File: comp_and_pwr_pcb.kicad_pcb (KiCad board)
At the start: 4 copper layers, 50 x 88.5 mm, 145 parts, among them IC1 TPS5430MDDAREP, IC2 ICM-42688-P, IC3 LTC4415EDHC#TRPBF, IC4 TPS259531DSGR, IC5 BMP388, IC6 W25Q32JVSSIQ, J1 USB4216-03-A, J10 Conn_01x02, J11 Conn_Coaxial, J12 Conn_Coaxial, J2 BATTERY_CONN, J3 SWD_CONN, J4 SERVO_CONN_01, J5 SERVO_CONN_02, J6 DM3AT-SF-PEJM5, J7 CAMERA_CONN_01, J8 CAMERA_CONN_02, J9 Conn_01x02, Q1 2N3904, Q2 BSS138, Q3 BSS138, Q4 BC847B, Q5 BC847B, Q6 MMBT3904, Q7 MMBT3904, SW1 SW_Push, SW2 SW_Push, U1 RP2040, U2 MAX-M10S, U3 MP2307DN-LF-Z, Y1 ABMM2-12.000MHZ-D1-T

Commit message: Changes
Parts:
- removed C14, C22: 10uF, Capacitor_SMD:C_0402_1005Metric
- removed C21, C25: 100nF, Capacitor_SMD:C_0402_1005Metric
- removed IC2: ICM-42688-P, ICM-42688-P:IIM42352
- removed JP4: SolderJumper_3_Open, Jumper:SolderJumper-3_P1.3mm_Open_Pad1.0x1.5mm
- removed Q7: MMBT3904, Package_TO_SOT_SMD:SOT-23
- added C26: 100nF, Capacitor_SMD:C_0402_1005Metric, F.Cu at (136.8, 152.5)
- added C27: 10uF, Capacitor_SMD:C_0402_1005Metric, F.Cu at (136.8, 151.0)
- added C31: 10uF, Capacitor_SMD:C_0402_1005Metric, F.Cu at (136.8, 144.5)
- added C32: 100nF, Capacitor_SMD:C_0402_1005Metric, F.Cu at (136.8, 145.8)
- added JP2: SolderJumper_3_Open, Jumper:SolderJumper-3_P1.3mm_Open_Pad1.0x1.5mm, F.Cu at (135.3, 141.5)
- added Q8: DMP3013SFV, Package_SON:Diodes_PowerDI3333-8, F.Cu at (116.5, 131.5)
- added U4: LSM6DSO, LSM6DSO:LGA14L, F.Cu at (135.8, 148.5)
- Q6: value MMBT3904 -> DMP3013SFV; footprint Package_TO_SOT_SMD:SOT-23 -> Package_SON:Diodes_PowerDI3333-8
- moved D3 6.02 mm to (115.0, 96.5)
- moved Q6 4.55 mm to (116.5, 136.0)
- moved J4 0.46 mm to (140.0, 109.0)
- moved D5 0.41 mm to (133.3, 94.0), turned to 180 degrees
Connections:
- Q6 pad 1: Net-(Q6-B) -> +BATT
- Q6 pad 3: Net-(J10-Pin_1) -> +BATT
- R58 pad 1: Net-(Q6-B) -> Net-(Q8-G)
- R62 pad 1: Net-(Q7-B) -> Net-(Q6-G)
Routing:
- net Net-(Q6-G): track 0.00 -> 11.0 mm
- net GND: track 267.5 -> 258.3 mm
- net Net-(IC2-AP_SDO_/_AP_AD0): track 7.78 -> 0.00 mm
- net Net-(JP2-C): track 0.00 -> 7.17 mm, vias 0 -> 2
- net Net-(Q8-G): track 0.00 -> 5.21 mm
- net +BATT: track 178.7 -> 182.7 mm, vias 5 -> 4
- net Net-(Q7-B): track 4.86 -> 1.34 mm, vias 2 -> 1
- net Net-(Q6-B): track 2.64 -> 0.00 mm
- net Net-(D3-A2): track 30.0 -> 28.0 mm, vias 0 -> 1
- net Net-(J10-Pin_1): track 56.7 -> 57.9 mm
- net /I2C_SCL: track 98.5 -> 99.6 mm, vias 6 -> 7
- net /SWDIO: track 44.7 -> 45.5 mm, vias 4 -> 5
- net Net-(J9-Pin_1): track 24.7 -> 25.5 mm
- net /WSP_SS: track 53.0 -> 53.6 mm
- net +3.3V: track 243.7 -> 244.2 mm, vias 10 -> 12
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
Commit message: added MPN and manufacturer
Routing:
- net Net-(Q7-B): track 1.34 -> 0.00 mm, vias 1 -> 0
- net (no net): track 0.00 -> 1.34 mm, vias 0 -> 1

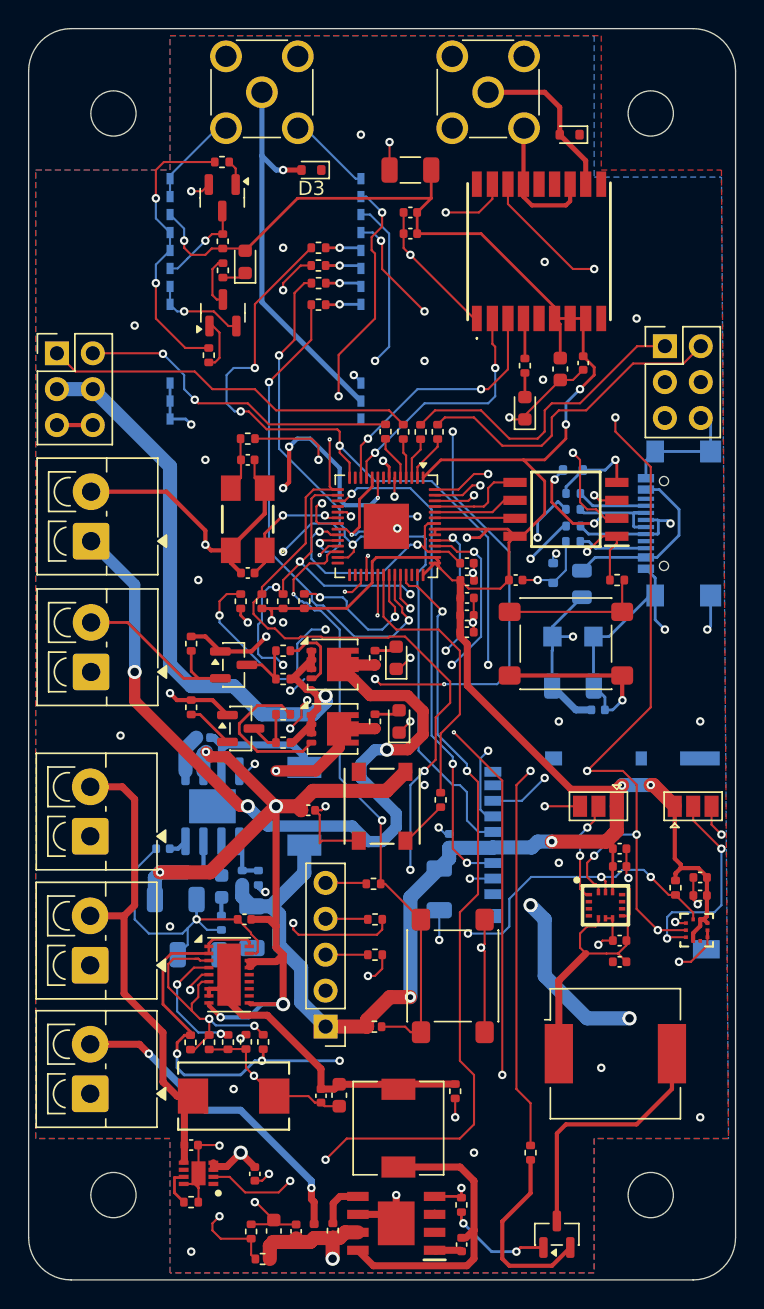
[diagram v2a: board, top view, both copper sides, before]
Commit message: Silkscreen added
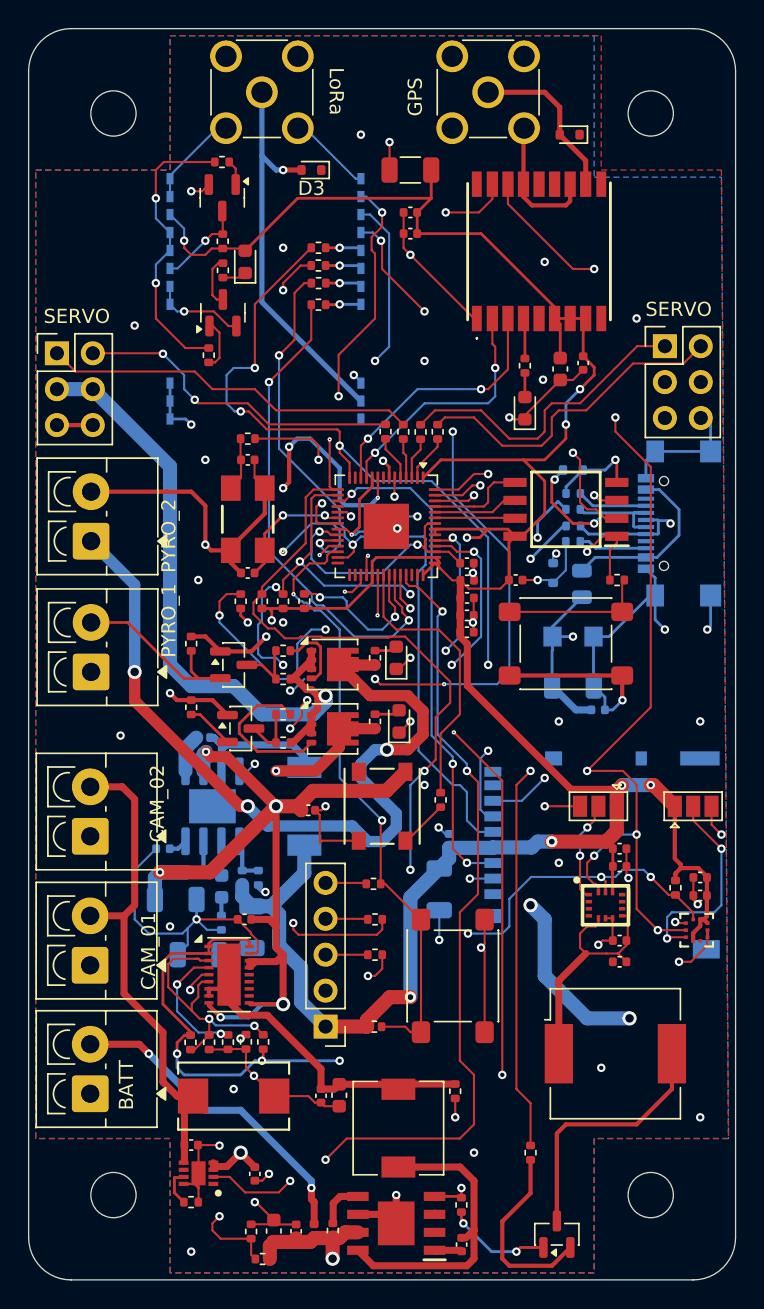
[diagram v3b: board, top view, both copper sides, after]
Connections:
- net Net-(D3-A2) renamed RF_NET
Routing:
- net GND: track 258.3 -> 259.3 mm
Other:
- board text added: "BATT"
- board text added: "CAM_01"
- board text added: "CAM_02"
- board text added: "GPS"
- board text added: "LoRa"
- board text added: "PYRO_1"
- board text added: "PYRO_2"
- board text added: "SERVO"
